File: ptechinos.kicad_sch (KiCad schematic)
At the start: 75 parts, among them J1 B+, J2 Battery, J3 B-, J4 AudioJack4, J5 Trackpad FPC, J6 OLED, SW1 SW_Power, SW2 Reset, U1 ProMicro

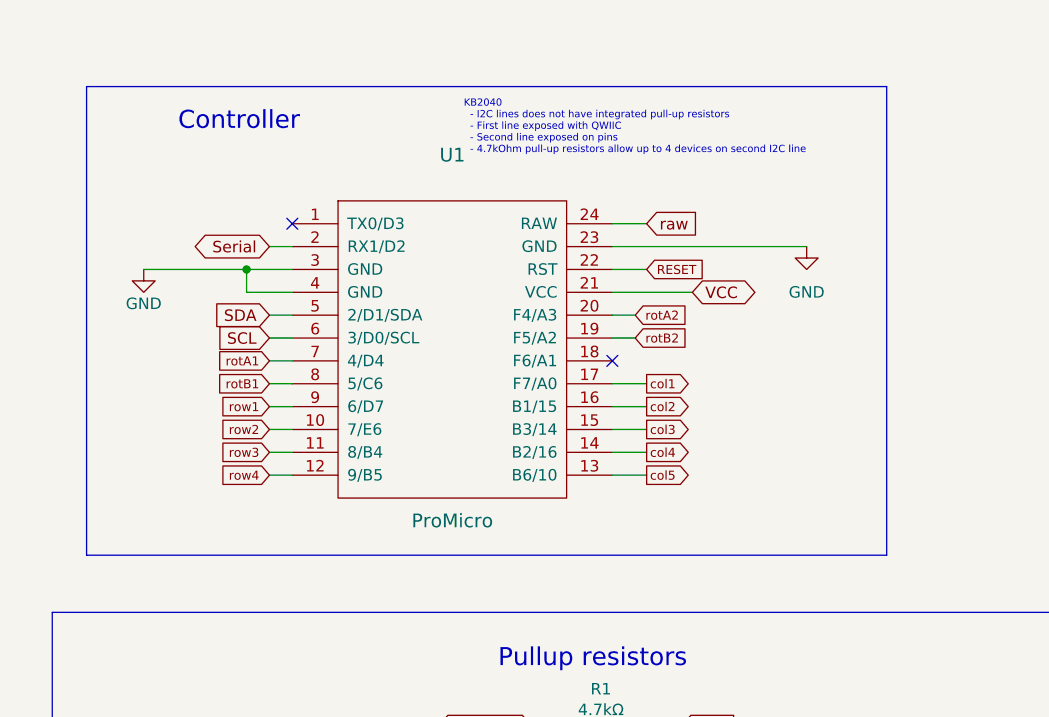
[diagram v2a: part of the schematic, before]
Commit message: ♻️ 🍱 - Add note about how to connect an SPI component.
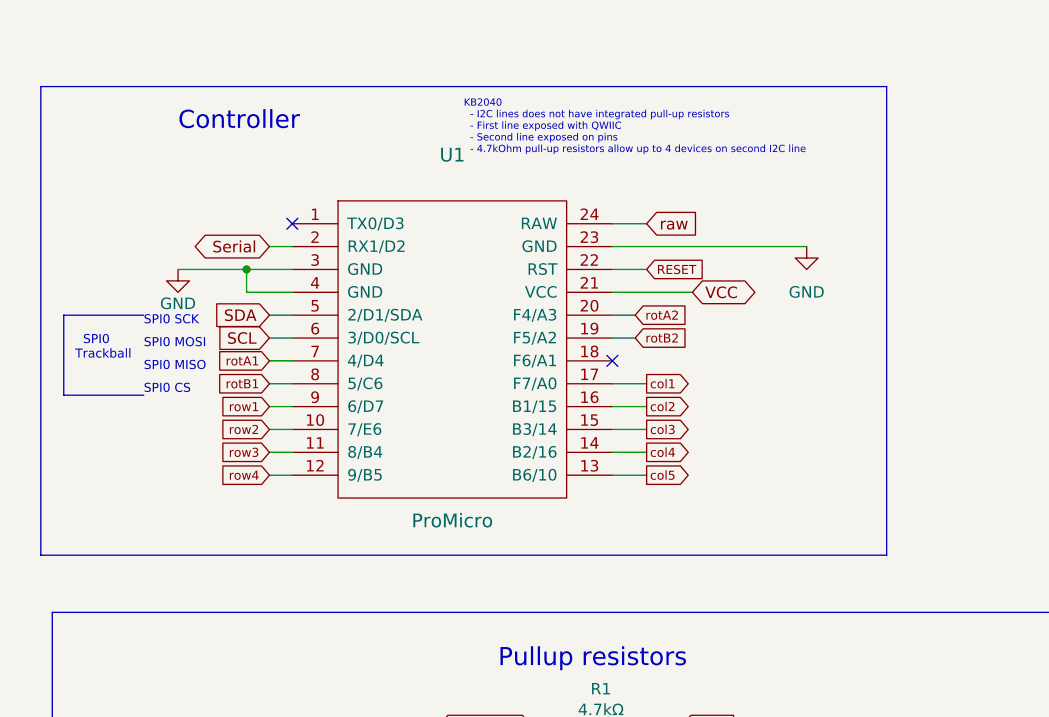
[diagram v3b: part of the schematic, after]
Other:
- note added: "SPI0 CS"
- note added: "SPI0 MISO"
- note added: "SPI0 MOSI"
- note added: "SPI0 SCK"
- note added: "SPI0 Trackball"
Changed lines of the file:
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@@
   (title_block
     (title "Ptechinos")
-    (date "2022-08-14")
+    (date "2022-08-24")
     (rev "0.6")
     (comment 1 "A crossover between Pteron36 and Balbuzard.")
@@
     (stroke (width 0) (type solid) (color 0 0 0 0))
   )
+  (polyline (pts (xy 27.94 54.61) (xy 19.05 54.61))
+    (stroke (width 0) (type default) (color 0 0 0 0))
+  )
   (wire (pts (xy 80.01 60.96) (xy 83.82 60.96))
     (stroke (width 0) (type default) (color 0 0 0 0))
@@
     (stroke (width 0) (type default) (color 0 0 0 0))
   )
-  (polyline (pts (xy 21.59 72.39) (xy 110.49 72.39))
+  (polyline (pts (xy 16.51 72.39) (xy 110.49 72.39))
     (stroke (width 0) (type default) (color 0 0 0 0))
   )
@@
     (stroke (width 0) (type default) (color 0 0 0 0))
   )
+  (polyline (pts (xy 19.05 45.72) (xy 19.05 54.61))
+    (stroke (width 0) (type default) (color 0 0 0 0))
+  )
   (wire (pts (xy 149.86 17.78) (xy 148.59 17.78))
     (stroke (width 0) (type default) (color 0 0 0 0))
@@
     (stroke (width 0) (type default) (color 0 0 0 0))
   )
-  (polyline (pts (xy 110.49 20.32) (xy 21.59 20.32))
+  (polyline (pts (xy 110.49 20.32) (xy 16.51 20.32))
     (stroke (width 0) (type default) (color 0 0 0 0))
   )
@@
     (stroke (width 0) (type default) (color 0 0 0 0))
   )
-  (wire (pts (xy 27.94 40.64) (xy 39.37 40.64))
+  (wire (pts (xy 31.75 40.64) (xy 39.37 40.64))
     (stroke (width 0) (type default) (color 0 0 0 0))
   )
@@
     (stroke (width 0) (type default) (color 0 0 0 0))
   )
-  (polyline (pts (xy 21.59 20.32) (xy 21.59 72.39))
+  (polyline (pts (xy 16.51 20.32) (xy 16.51 72.39))
+    (stroke (width 0) (type default) (color 0 0 0 0))
+  )
+  (polyline (pts (xy 19.05 45.72) (xy 27.94 45.72))
     (stroke (width 0) (type default) (color 0 0 0 0))
   )
@@
     (stroke (width 0) (type default) (color 0 0 0 0))
   )
+  (text "SPI0 MISO" (at 27.94 52.07 0)
+    (effects (font (size 1 1)) (justify left bottom))
+  )
   (text "Holes" (at 142.24 163.83 0)
     (effects (font (size 2 2)) (justify left bottom))
+  )
+  (text "SPI0 CS" (at 27.94 54.61 0)
+    (effects (font (size 1 1)) (justify left bottom))
   )
   (text "KB2040\n  - I2C lines does not have integrated pull-up resistors\n  - First line exposed with QWIIC\n  - Second line exposed on pins\n  - 4.7kOhm pull-up resistors allow up to 4 devices on second I2C line"
@@
   (text "Trackpad\n" (at 90.17 113.03 0)
     (effects (font (size 2 2)) (justify left bottom))
+  )
+  (text "SPI0 MOSI" (at 27.94 49.53 0)
+    (effects (font (size 1 1)) (justify left bottom))
+  )
+  (text "SPI0 SCK" (at 27.94 46.99 0)
+    (effects (font (size 1 1)) (justify left bottom))
+  )
+  (text "  SPI0\nTrackball" (at 20.32 50.8 0)
+    (effects (font (size 1 1)) (justify left bottom))
   )
   (text "Switches" (at 260.35 39.37 180)
@@
     (pin "2")
   )
-  (symbol (lib_id "power:GND") (at 27.94 40.64 0) (mirror y) (unit 1)
-    (in_bom yes) (on_board yes)
-    (property "Reference" "#PWR01" (id 0) (at 27.94 46.99 0)
-      (effects (font (size 1.27 1.27)) hide)
-    )
-    (property "Value" "GND" (id 1) (at 27.94 44.45 0))
-    (property "Footprint" "" (id 2) (at 27.94 40.64 0)
-      (effects (font (size 1.27 1.27)) hide)
-    )
-    (property "Datasheet" "" (id 3) (at 27.94 40.64 0)
-      (effects (font (size 1.27 1.27)) hide)
-    )
+  (symbol (lib_id "power:GND") (at 31.75 40.64 0) (mirror y) (unit 1)
+    (in_bom yes) (on_board yes)
+    (property "Reference" "#PWR01" (id 0) (at 31.75 46.99 0)
+      (effects (font (size 1.27 1.27)) hide)
+    )
+    (property "Value" "GND" (id 1) (at 31.75 44.45 0))
+    (property "Footprint" "" (id 2) (at 31.75 40.64 0)
+      (effects (font (size 1.27 1.27)) hide)
+    )
+    (property "Datasheet" "" (id 3) (at 31.75 40.64 0)
+      (effects (font (size 1.27 1.27)) hide)
+    )

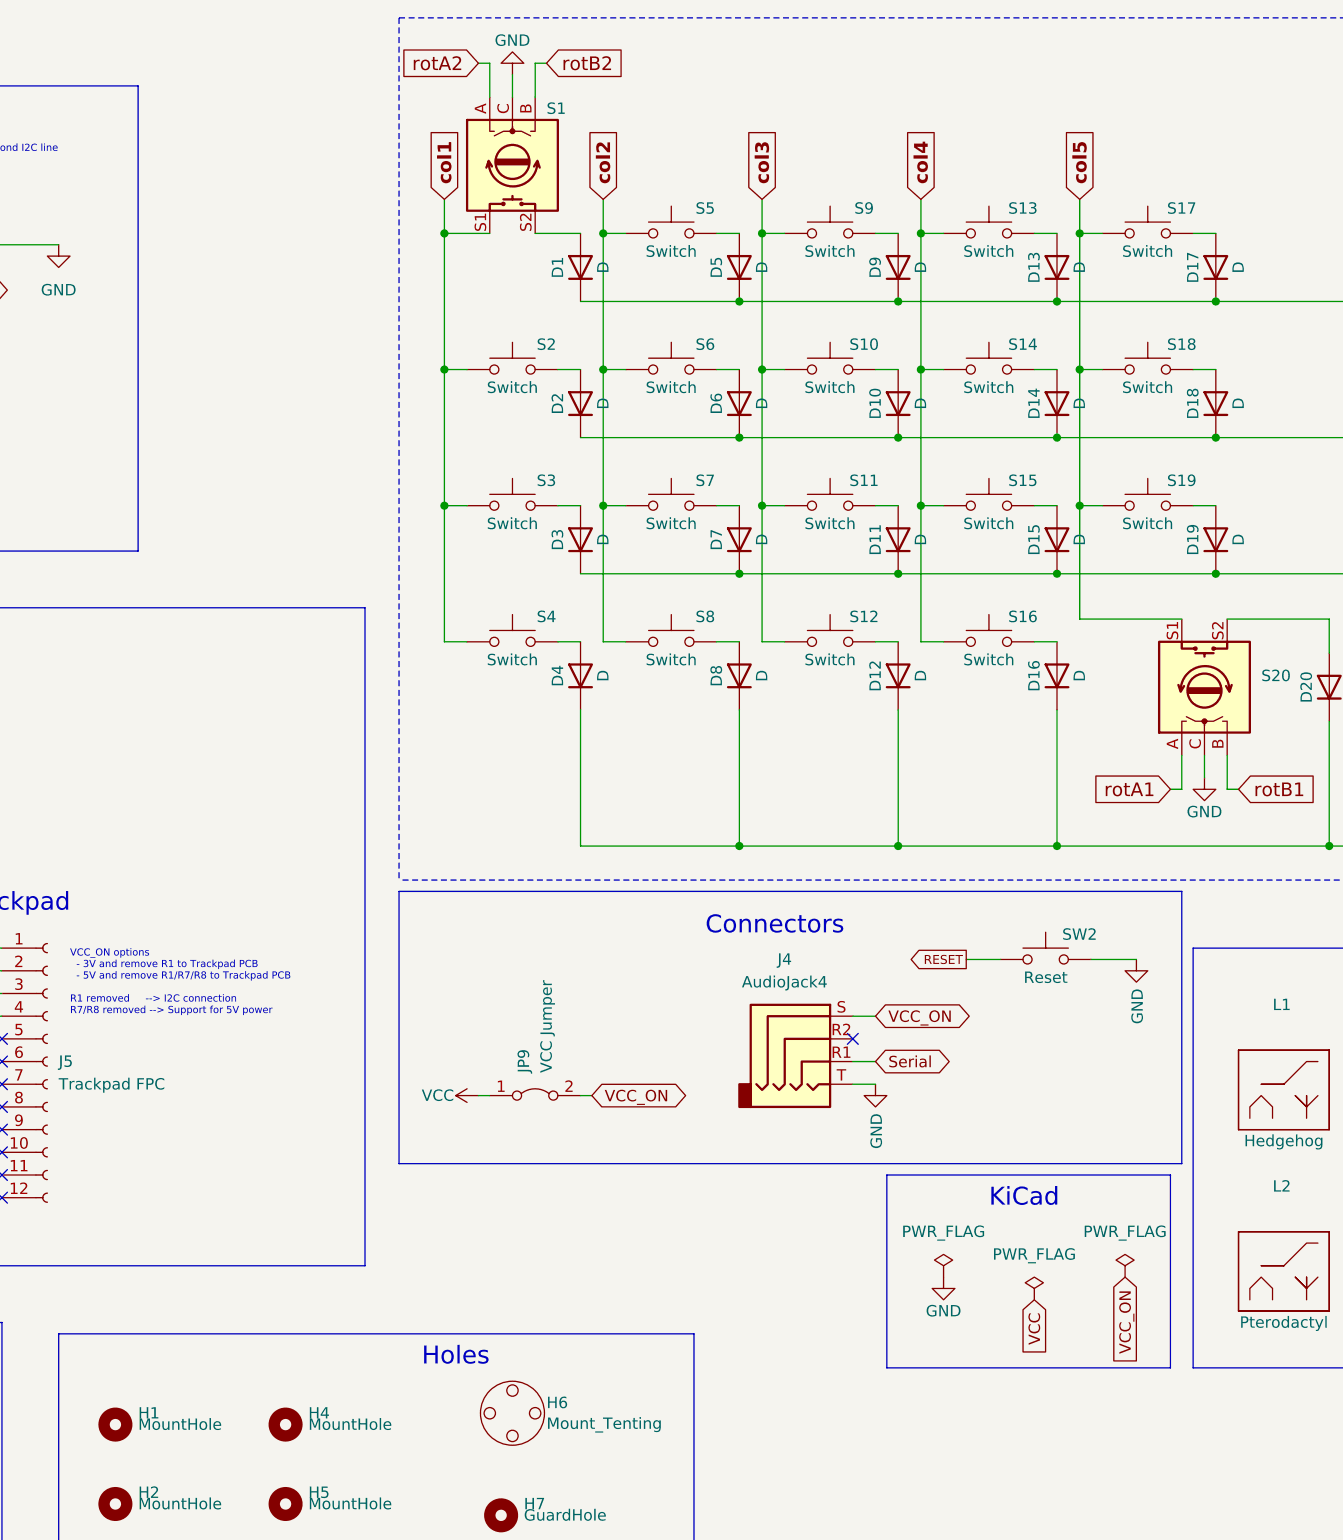
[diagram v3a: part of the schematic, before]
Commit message: ♻️ 🚧 - Update components organization around the MCU to make some place for a pogo 4 pins connector. This connector is an alternative of TRRS to connect both halves together. This connection is safer for two main reasons: shorts cannot happens if removed during use, cable will gently disconnect when rip off. This connector will also be used later to allow to switch between split and unsplit configuration.
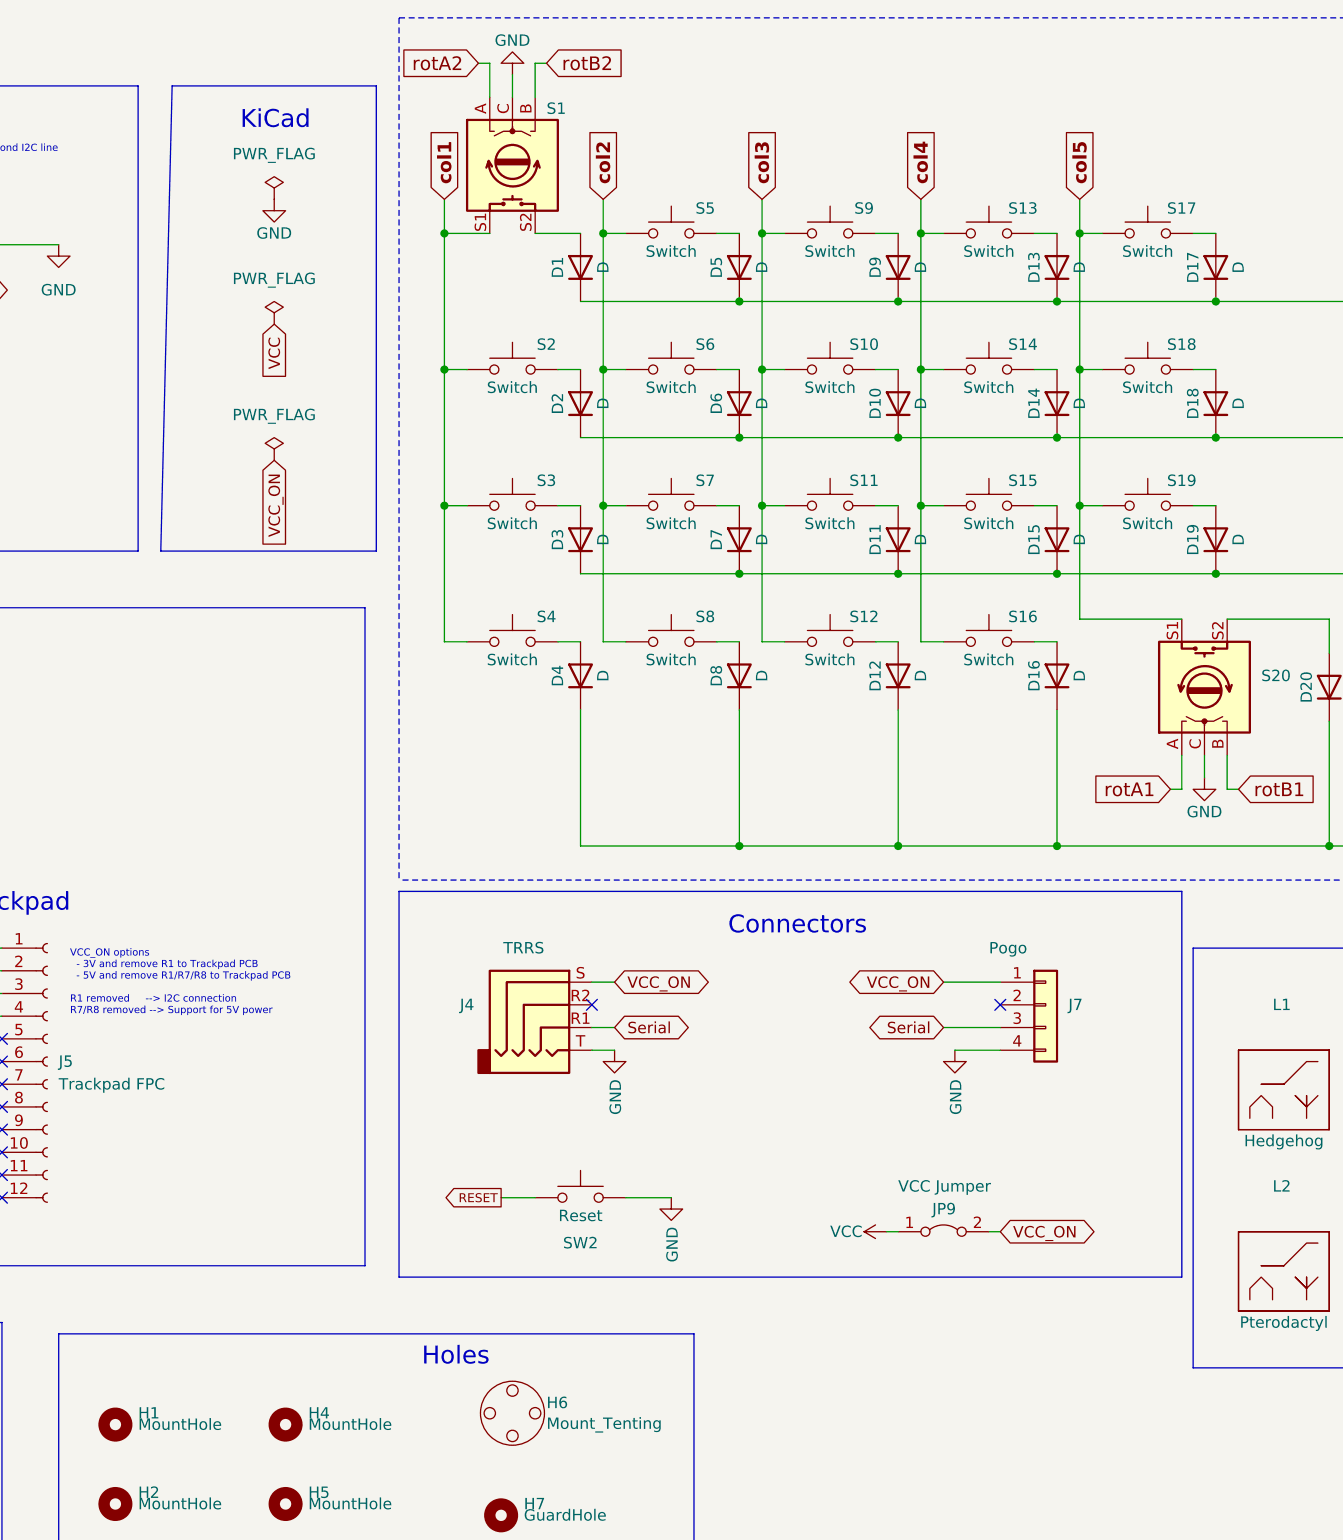
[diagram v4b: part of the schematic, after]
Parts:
- added J7: Pogo, ptechinos:PinSocket_1x04_P2.54mm_Vertical, symbol Connector_Generic:Conn_01x04
- J4: value AudioJack4 -> TRRS
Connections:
- net GND: now also J7.4 (Pin_4)
- net Serial: now also J7.3 (Pin_3)
- net VCC_ON: now also J7.1 (Pin_1)
- no-connect marks 12 -> 13
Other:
- moved on the sheet: J4, JP9, SW2

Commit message: ⬆️ - Update drawing an PCB dates (previews not regenerated).
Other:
- note added: "Pin 18 as Row5 Mouse buttons (L, M, R)"
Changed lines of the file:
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@@
   (title_block
     (title "Ptechinos")
-    (date "2022-08-24")
+    (date "2022-09-04")
     (rev "0.6")
     (comment 1 "A crossover between Pteron36 and Balbuzard.")
@@
     (effects (font (size 0.8 0.8)) (justify left bottom))
   )
+  (text "Pin 18 as Row5\nMouse buttons (L, M, R)" (at 88.9 52.07 0)
+    (effects (font (size 1 1)) (justify left bottom))
+  )
   (text "Connectors" (at 176.53 115.57 0)

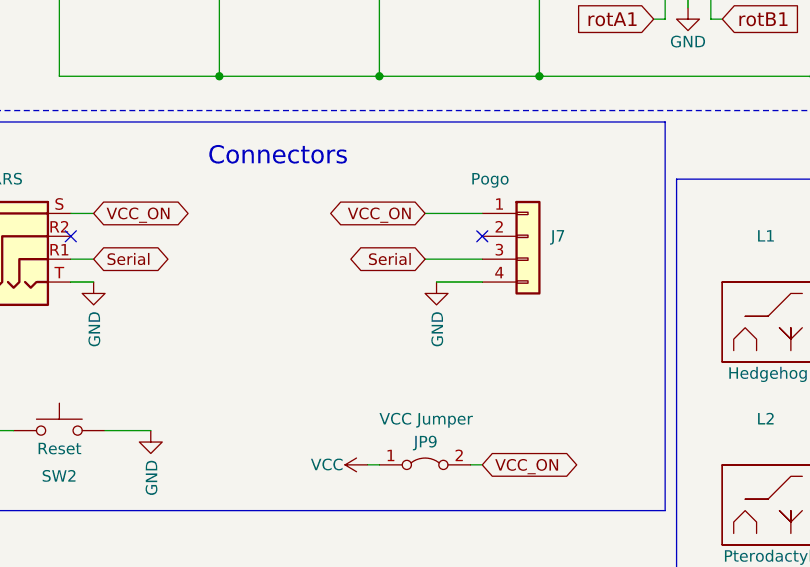
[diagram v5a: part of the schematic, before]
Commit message: ♻️ - Move Reset under the Trackpad to free space for pogo magnetic connectors. Update pogo schematic pins assignation to make it compatible with 3 pins pogo as well (used pins are now 1, 2, 3).
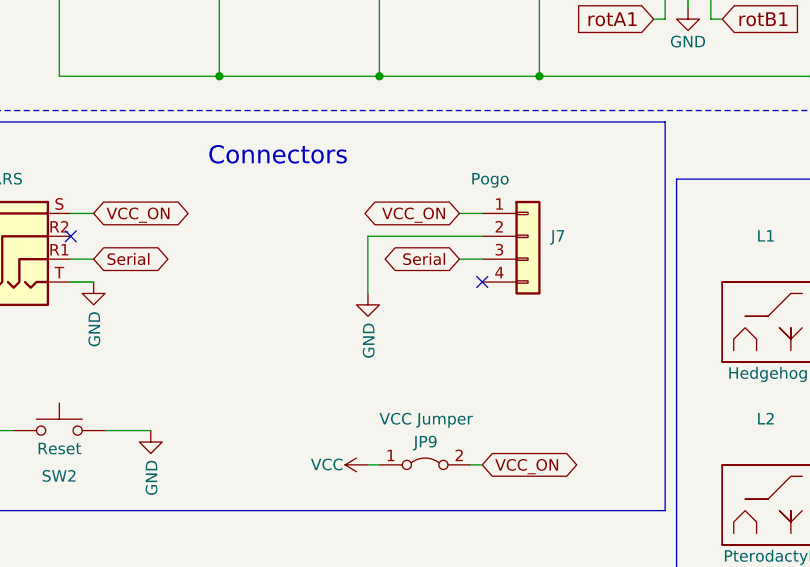
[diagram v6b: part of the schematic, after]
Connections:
- net GND: now also J7.2 (Pin_2); no longer J7.4 (Pin_4)
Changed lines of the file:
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@@
   (no_connect (at 95.25 142.24))
   (no_connect (at 95.25 139.7))
-  (no_connect (at 207.01 123.19))
+  (no_connect (at 207.01 128.27))
   (no_connect (at 44.45 35.56))
   (no_connect (at 161.29 123.19))
@@
     (stroke (width 0) (type default) (color 0 0 0 0))
   )
-  (wire (pts (xy 200.66 125.73) (xy 207.01 125.73))
+  (wire (pts (xy 204.47 125.73) (xy 207.01 125.73))
     (stroke (width 0) (type default) (color 0 0 0 0))
   )
@@
     (stroke (width 0) (type default) (color 0 0 0 0))
   )
-  (wire (pts (xy 200.66 120.65) (xy 207.01 120.65))
+  (wire (pts (xy 204.47 120.65) (xy 207.01 120.65))
     (stroke (width 0) (type default) (color 0 0 0 0))
   )
@@
     (stroke (width 0) (type default) (color 0 0 0 0))
   )
+  (wire (pts (xy 194.31 123.19) (xy 194.31 129.54))
+    (stroke (width 0) (type default) (color 0 0 0 0))
+  )
   (wire (pts (xy 215.9 80.01) (xy 227.33 80.01))
     (stroke (width 0) (type default) (color 0 0 0 0))
@@
     (stroke (width 0) (type default) (color 0 0 0 0))
   )
-  (wire (pts (xy 201.93 128.27) (xy 207.01 128.27))
-    (stroke (width 0) (type default) (color 0 0 0 0))
-  )
   (wire (pts (xy 87.63 91.44) (xy 81.28 91.44))
     (stroke (width 0) (type default) (color 0 0 0 0))
@@
   )
   (wire (pts (xy 36.83 168.91) (xy 36.83 177.8))
+    (stroke (width 0) (type default) (color 0 0 0 0))
+  )
+  (wire (pts (xy 207.01 123.19) (xy 194.31 123.19))
     (stroke (width 0) (type default) (color 0 0 0 0))
   )
@@
     )
   )
-  (global_label "Serial" (shape bidirectional) (at 200.66 125.73 180) (fields_autoplaced)
-    (effects (font (size 1.27 1.27)) (justify right))
-    (property "Intersheet References" "${INTERSHEET_REFS}" (id 0) (at 192.7436 125.6506 0)
+  (global_label "Serial" (shape bidirectional) (at 204.47 125.73 180) (fields_autoplaced)
+    (effects (font (size 1.27 1.27)) (justify right))
+    (property "Intersheet References" "${INTERSHEET_REFS}" (id 0) (at 196.5536 125.6506 0)
       (effects (font (size 1.27 1.27)) (justify right) hide)
     )
@@
     )
   )
-  (global_label "VCC_ON" (shape bidirectional) (at 200.66 120.65 180) (fields_autoplaced)
-    (effects (font (size 1.27 1.27)) (justify right))
-    (property "Intersheet References" "${INTERSHEET_REFS}" (id 0) (at 190.9898 120.5706 0)
+  (global_label "VCC_ON" (shape bidirectional) (at 204.47 120.65 180) (fields_autoplaced)
+    (effects (font (size 1.27 1.27)) (justify right))
+    (property "Intersheet References" "${INTERSHEET_REFS}" (id 0) (at 194.7998 120.5706 0)
       (effects (font (size 1.27 1.27)) (justify right) hide)
     )
@@
     (pin "2")
   )
-  (symbol (lib_id "power:GND") (at 201.93 128.27 0) (unit 1)
-    (in_bom yes) (on_board yes)
-    (property "Reference" "#PWR013" (id 0) (at 201.93 134.62 0)
-      (effects (font (size 1.27 1.27)) hide)
-    )
-    (property "Value" "GND" (id 1) (at 202.057 131.5212 90)
+  (symbol (lib_id "power:GND") (at 194.31 129.54 0) (unit 1)
+    (in_bom yes) (on_board yes)
+    (property "Reference" "#PWR013" (id 0) (at 194.31 135.89 0)
+      (effects (font (size 1.27 1.27)) hide)
+    )
+    (property "Value" "GND" (id 1) (at 194.437 132.7912 90)
       (effects (font (size 1.27 1.27)) (justify right))
     )
-    (property "Footprint" "" (id 2) (at 201.93 128.27 0)
-      (effects (font (size 1.27 1.27)) hide)
-    )
-    (property "Datasheet" "" (id 3) (at 201.93 128.27 0)
-      (effects (font (size 1.27 1.27)) hide)
-    )
+    (property "Footprint" "" (id 2) (at 194.31 129.54 0)
+      (effects (font (size 1.27 1.27)) hide)
+    )
+    (property "Datasheet" "" (id 3) (at 194.31 129.54 0)
+      (effects (font (size 1.27 1.27)) hide)
+    )
